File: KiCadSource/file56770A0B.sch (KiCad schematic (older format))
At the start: 60 parts, among them Q1 BSS138BKS, Q2 BSS138BKS, U1 ADA4817-1, U2 ADA4817-1

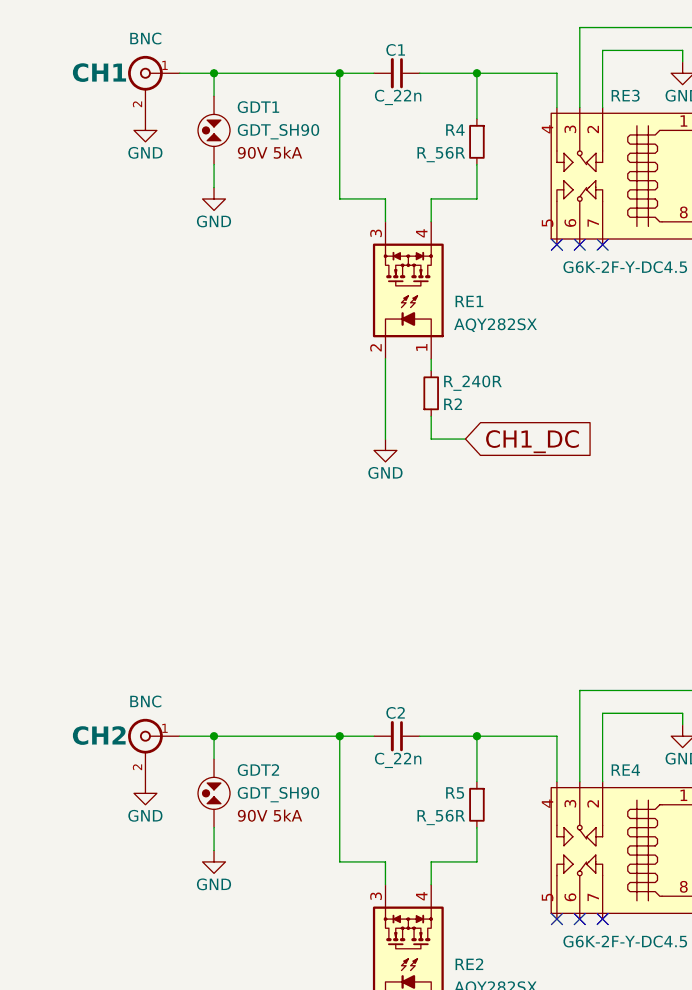
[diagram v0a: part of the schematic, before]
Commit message: first production run, digital GPIOs, replaced parts (see CHANGES.txt)
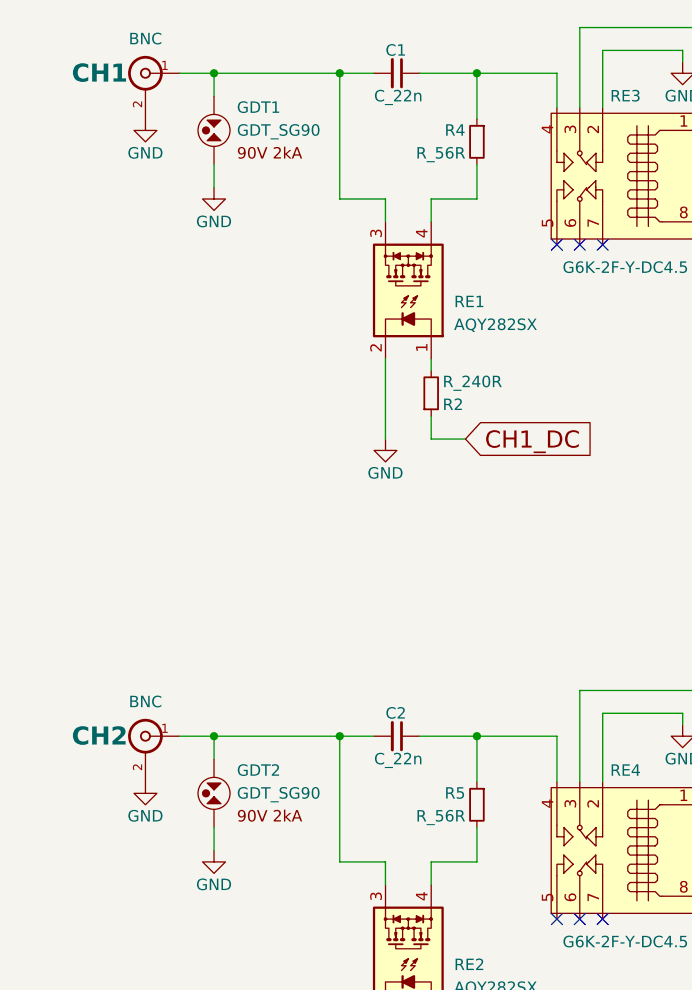
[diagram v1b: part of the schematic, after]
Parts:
- removed GDT1, GDT2: GDT_SH90, ScopefunPackagesLibrary:GDT_SH, symbol GDT_SH90
- added GDT1, GDT2: GDT_SG90, ScopefunPackagesLibrary:GDT_SG, symbol GDT_SG90
- C11, C13: footprint ScopefunPackagesLibrary:0603 -> ScopefunPackagesLibrary:C_0603; Description MLCC - SMD/SMT 0603 100V C0G 2% -> MLCC - SMD/SMT 0603 50V C0G 2%
- C12, C14, C4, C6: footprint ScopefunPackagesLibrary:0603 -> ScopefunPackagesLibrary:C_0603
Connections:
- net GND: now also GDT1.2, GDT2.2
- net at C1.2, CH1.1 (In), RE1.3: now also GDT1.1
- net at C2.2, CH2.1 (In), RE2.3: now also GDT2.1
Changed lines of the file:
@@
 F 0 "C4" H 4960 2220 50  0000 L CNN
 F 1 "C_360p" H 4960 2070 50  0000 L CNN
-F 2 "ScopefunPackagesLibrary:0603" H 4950 1950 50  0001 C CNN
+F 2 "ScopefunPackagesLibrary:C_0603" H 4950 1950 50  0001 C CNN
 F 3 "" H 4960 2220 50  0001 C CNN
 F 4 "C0603C361G5GACTU" H 4950 2350 60  0001 C CNN "MFG Part#"
@@
 F 0 "C6" H 4960 5120 50  0000 L CNN
 F 1 "C_360p" H 4960 4970 50  0000 L CNN
-F 2 "ScopefunPackagesLibrary:0603" H 4950 4850 50  0001 C CNN
+F 2 "ScopefunPackagesLibrary:C_0603" H 4950 4850 50  0001 C CNN
 F 3 "" H 4960 5120 50  0001 C CNN
 F 4 "C0603C361G5GACTU" H 4950 5250 60  0001 C CNN "MFG Part#"
@@
 F 0 "C11" H 8360 1420 50  0000 L CNN
 F 1 "C_390p" H 8360 1270 50  0000 L CNN
-F 2 "ScopefunPackagesLibrary:0603" H 8350 1150 50  0001 C CNN
+F 2 "ScopefunPackagesLibrary:C_0603" H 8350 1150 50  0001 C CNN
 F 3 "" H 8360 1420 50  0001 C CNN
 F 4 "VJ0603A391GXAPW1BC" H 8350 1550 60  0001 C CNN "MFG Part#"
-F 5 "MLCC - SMD/SMT 0603 100V C0G 2%" H 8350 1650 60  0001 C CNN "Description"
+F 5 "MLCC - SMD/SMT 0603 50V C0G 2%" H 8350 1650 60  0001 C CNN "Description"
 	1    8350 1350
 	1    0    0    -1
@@
 F 0 "C13" H 8360 4320 50  0000 L CNN
 F 1 "C_390p" H 8360 4170 50  0000 L CNN
-F 2 "ScopefunPackagesLibrary:0603" H 8350 4050 50  0001 C CNN
+F 2 "ScopefunPackagesLibrary:C_0603" H 8350 4050 50  0001 C CNN
 F 3 "" H 8360 4320 50  0001 C CNN
 F 4 "VJ0603A391GXAPW1BC" H 8350 4450 60  0001 C CNN "MFG Part#"
-F 5 "MLCC - SMD/SMT 0603 100V C0G 2%" H 8350 4550 60  0001 C CNN "Description"
+F 5 "MLCC - SMD/SMT 0603 50V C0G 2%" H 8350 4550 60  0001 C CNN "Description"
 	1    8350 4250
-	1    0    0    -1
-$EndComp
-$Comp
-L GDT_SH90 GDT2
-U 1 1 5BA058D4
-P 1250 3950
-F 0 "GDT2" H 1350 4050 50  0000 L CNN
-F 1 "GDT_SH90" H 1350 3950 50  0000 L CNN
-F 2 "ScopefunPackagesLibrary:GDT_SH" H 1250 3700 50  0001 C CNN
-F 3 "https://www.littelfuse.com/~/media/electronics/datasheets/gas_discharge_tubes/littelfuse_gdt_sh_datasheet.pdf.pdf" H 1250 3600 50  0001 C CNN
-F 4 "SH90" H 1250 4200 60  0001 C CNN "MFG Part#"
-F 5 "Gas Discharge Tube - GDT 90V 5kA 0.7pF" H 1250 4300 60  0001 C CNN "Description"
-	1    1250 3950
 	1    0    0    -1
 $EndComp
@@
 	-1   0    0    -1
 $EndComp
-$Comp
-L GDT_SH90 GDT1
-U 1 1 5BA067C9
-P 1250 1050
-F 0 "GDT1" H 1350 1150 50  0000 L CNN
-F 1 "GDT_SH90" H 1350 1050 50  0000 L CNN
-F 2 "ScopefunPackagesLibrary:GDT_SH" H 1250 800 50  0001 C CNN
-F 3 "https://www.littelfuse.com/~/media/electronics/datasheets/gas_discharge_tubes/littelfuse_gdt_sh_datasheet.pdf.pdf" H 1250 700 50  0001 C CNN
-F 4 "SH90" H 1250 1300 60  0001 C CNN "MFG Part#"
-F 5 "Gas Discharge Tube - GDT 90V 5kA 0.7pF" H 1250 1400 60  0001 C CNN "Description"
-	1    1250 1050
-	1    0    0    -1
-$EndComp
 Wire Wire Line
 	1250 1200 1250 1300
@@
 F 0 "C14" H 8360 5120 50  0000 L CNN
 F 1 "C_0603" H 8360 4970 50  0000 L CNN
-F 2 "ScopefunPackagesLibrary:0603" H 8350 4900 50  0001 C CNN
+F 2 "ScopefunPackagesLibrary:C_0603" H 8350 4900 50  0001 C CNN
 F 3 "" H 8360 5120 50  0001 C CNN
 F 4 "Not populated" H 8350 5200 50  0001 C CNN "Description"
@@
 F 0 "C12" H 8360 2220 50  0000 L CNN
 F 1 "C_0603" H 8360 2070 50  0000 L CNN
-F 2 "ScopefunPackagesLibrary:0603" H 8350 2000 50  0001 C CNN
+F 2 "ScopefunPackagesLibrary:C_0603" H 8350 2000 50  0001 C CNN
 F 3 "" H 8360 2220 50  0001 C CNN
 F 4 "Not populated" H 8350 2300 50  0001 C CNN "Description"
@@
 	1    0    0    -1
 $EndComp
+$Comp
+L GDT_SG90 GDT1
+U 1 1 5D33912B
+P 1250 1050
+F 0 "GDT1" H 1350 1150 50  0000 L CNN
+F 1 "GDT_SG90" H 1350 1050 50  0000 L CNN
+F 2 "ScopefunPackagesLibrary:GDT_SG" H 1250 800 50  0001 C CNN
+F 3 "https://www.littelfuse.com/~/media/electronics/datasheets/gas_discharge_tubes/littelfuse_gdt_sg_datasheet.pdf.pdf" H 1250 700 50  0001 C CNN
+F 4 "SG90" H 1250 1300 60  0001 C CNN "MFG Part#"
+F 5 "Gas Discharge Tube - GDT 90V 2kA <1.0 pF" H 1250 1400 60  0001 C CNN "Description"
+	1    1250 1050
+	1    0    0    -1
+$EndComp
+$Comp
+L GDT_SG90 GDT2
+U 1 1 5D339314
+P 1250 3950
+F 0 "GDT2" H 1350 4050 50  0000 L CNN
+F 1 "GDT_SG90" H 1350 3950 50  0000 L CNN
+F 2 "ScopefunPackagesLibrary:GDT_SG" H 1250 3700 50  0001 C CNN
+F 3 "https://www.littelfuse.com/~/media/electronics/datasheets/gas_discharge_tubes/littelfuse_gdt_sg_datasheet.pdf.pdf" H 1250 3600 50  0001 C CNN
+F 4 "SG90" H 1250 4200 60  0001 C CNN "MFG Part#"
+F 5 "Gas Discharge Tube - GDT 90V 2kA <1.0 pF" H 1250 4300 60  0001 C CNN "Description"
+	1    1250 3950
+	1    0    0    -1
+$EndComp
